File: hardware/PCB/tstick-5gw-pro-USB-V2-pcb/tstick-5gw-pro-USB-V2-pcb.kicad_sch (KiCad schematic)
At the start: 66 parts, among them J1 USB_C_Receptacle_USB2.0, Q1 BSS138, Q2 BSS138, Q3 BSS138, SW1 PTS810 SJM Switch, SW2 PTS810 SJM Switch, U1 USBLC6-2P6, U2 MCP73871, U3 NCP167AMX330TBG, U4 NCP167AMX180TBG

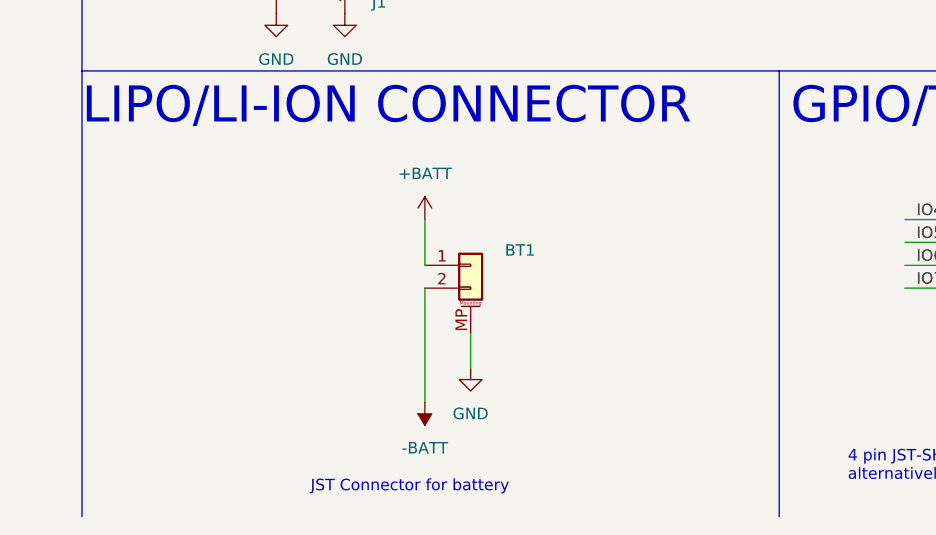
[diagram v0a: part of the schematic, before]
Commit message: updated pcb BOM, switched buttons to smaller 3x2mm buttons
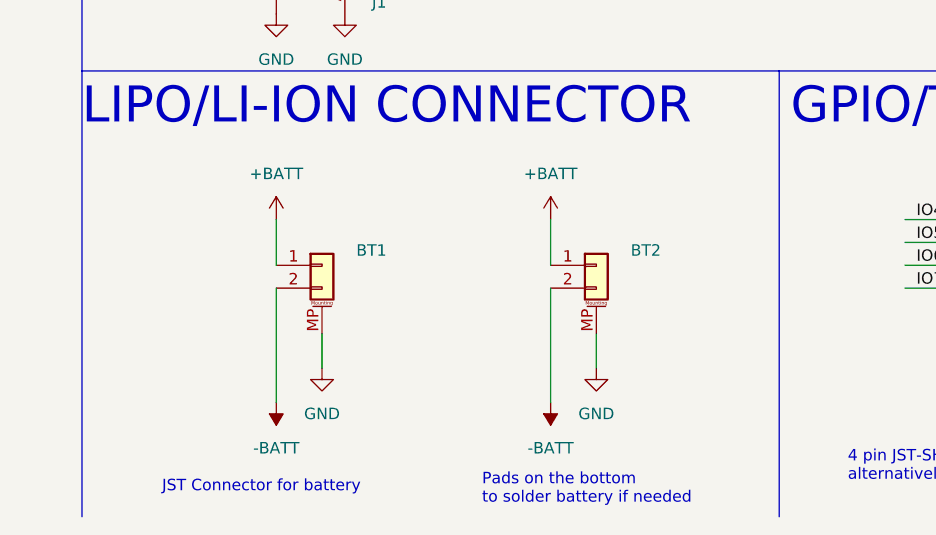
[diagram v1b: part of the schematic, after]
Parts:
- added BT2: JST-PH-1x02-2.000mm, Connector_JST:JST_PH_B2B-PH-SM4-TB_1x02-1MP_P2.00mm_Vertical, symbol Connector_Generic_MountingPin:Conn_01x02_MountingPin
- SW1, SW2: value PTS810 SJM Switch -> B3U-1000P; footprint Button_Switch_SMD:SW_SPST_PTS810 -> Button_Switch_SMD:SW_SPST_B3U-1000P; Manufacturer C&K -> Omron Electronics Inc-EMC Div; Mfg Part # PTS810 SJM 250 SMTR LFS -> B3U-1000P
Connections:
- net +BATT: now also BT2.1 (Pin_1)
- net -BATT: now also BT2.2 (Pin_2)
- net GND: now also BT2.MP (MountPin)
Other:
- note added: "Pads on the bottom to solder battery if needed"
- moved on the sheet: BT1

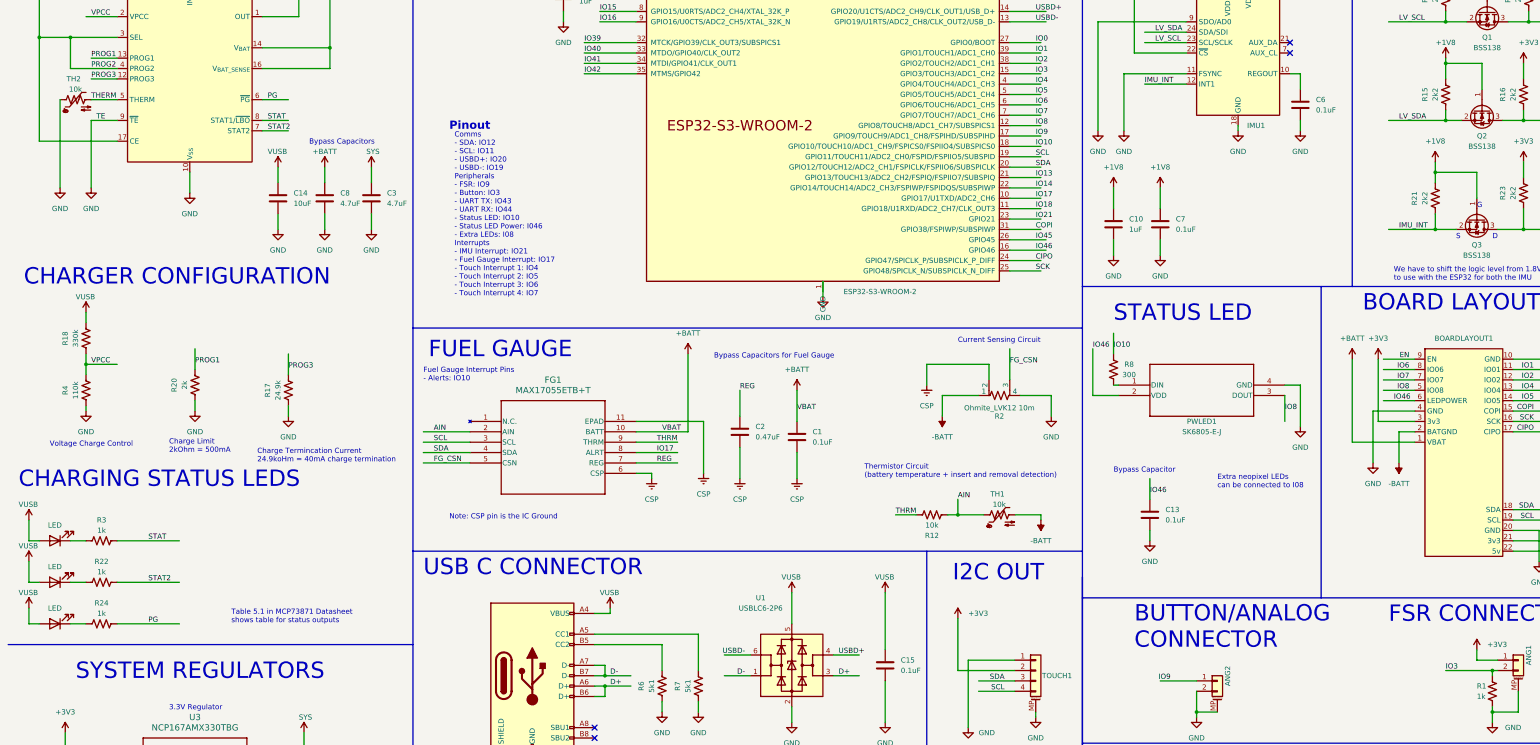
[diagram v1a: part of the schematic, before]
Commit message: updated board flash size, added button interrupt, removed serial print
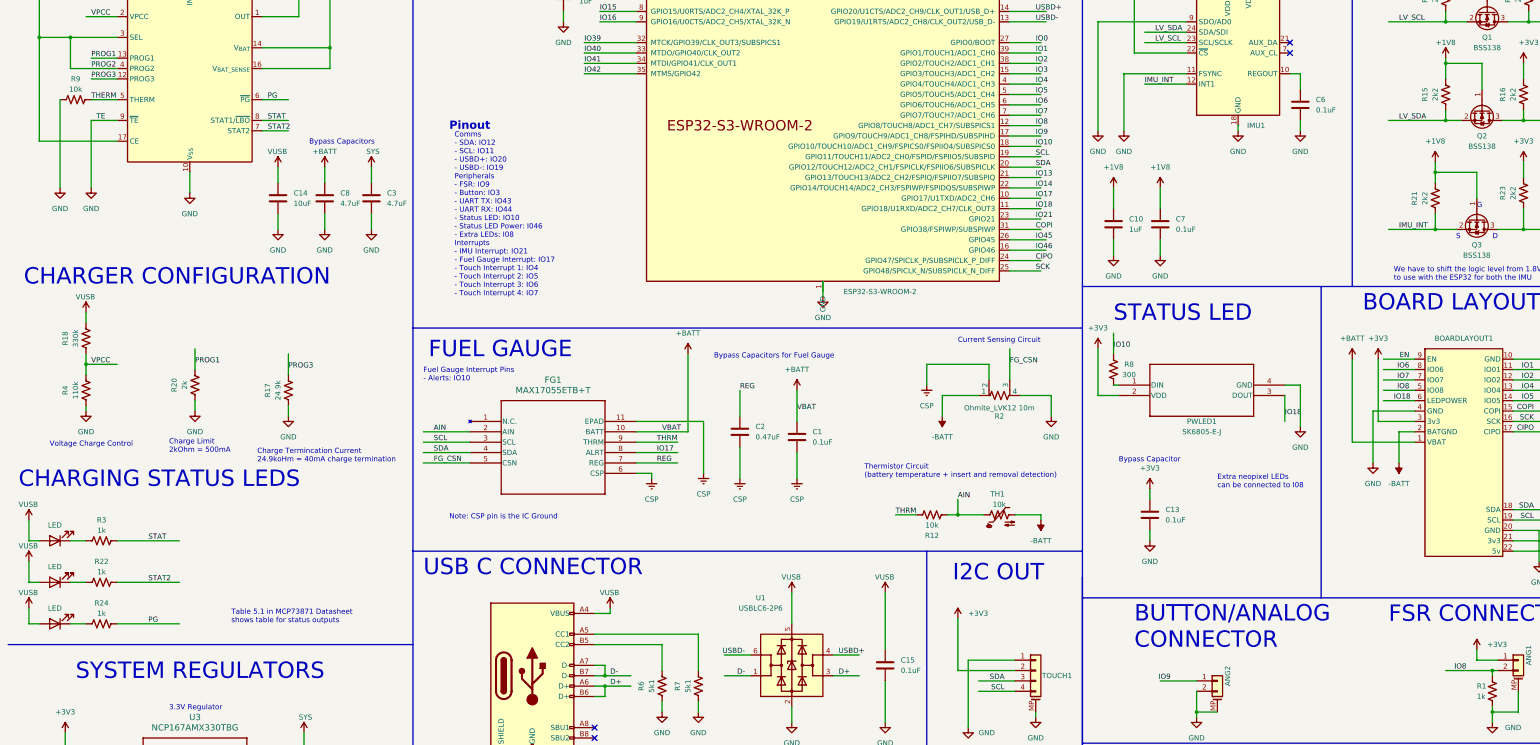
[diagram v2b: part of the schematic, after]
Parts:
- removed TH2: 10k, Resistor_SMD:R_0201_0603Metric, symbol Device:Thermistor_NTC_US
- added R9: 10k, Resistor_SMD:R_0201_0603Metric, symbol Device:R_US
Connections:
- net +3V3: now also C13.1, PWLED1.2 (VDD)
- net GND: now also R9.1
- net IO18: now also BOARDLAYOUT1.6 (LEDPOWER), PWLED1.3 (DOUT)
- net IO3: no longer ANG1.2 (Pin_2), R1.1
- net IO46: no longer BOARDLAYOUT1.6 (LEDPOWER), C13.1, PWLED1.2 (VDD)
- net IO8: now also ANG1.2 (Pin_2), R1.1; no longer PWLED1.3 (DOUT)
- net THERM: now also R9.2
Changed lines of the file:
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@@
     (stroke (width 0) (type default))
   )
-  (wire (pts (xy 276.86 125.73) (xy 276.86 137.16))
+  (wire (pts (xy 278.13 125.73) (xy 278.13 137.16))
     (stroke (width 0) (type default))
   )
@@
     (stroke (width 0) (type default))
   )
-  (wire (pts (xy 290.83 157.48) (xy 290.83 162.56))
+  (wire (pts (xy 290.83 160.02) (xy 290.83 162.56))
     (stroke (width 0) (type default))
   )
@@
     (stroke (width 0) (type default))
   )
-  (wire (pts (xy 276.86 137.16) (xy 283.21 137.16))
+  (wire (pts (xy 278.13 137.16) (xy 283.21 137.16))
     (stroke (width 0) (type default))
   )
@@
     (effects (font (size 1.27 1.27)) (justify left bottom))
   )
-  (text "Bypass Capacitor" (at 281.94 156.21 0)
+  (text "Bypass Capacitor" (at 283.21 153.67 0)
     (effects (font (size 1.27 1.27)) (justify left bottom))
   )
@@
     (effects (font (size 1.27 1.27)) (justify left bottom))
   )
-  (label "IO8" (at 323.85 140.97 0) (fields_autoplaced)
-    (effects (font (size 1.27 1.27)) (justify left bottom))
-  )
   (label "IO3" (at 262.89 58.42 0) (fields_autoplaced)
     (effects (font (size 1.27 1.27)) (justify left bottom))
@@
     (effects (font (size 1.27 1.27)) (justify left bottom))
   )
-  (label "IO46" (at 350.52 138.43 0) (fields_autoplaced)
-    (effects (font (size 1.27 1.27)) (justify left bottom))
-  )
   (label "SCK" (at 262.89 106.68 0) (fields_autoplaced)
     (effects (font (size 1.27 1.27)) (justify left bottom))
@@
     (effects (font (size 1.27 1.27)) (justify left bottom))
   )
-  (label "IO46" (at 290.83 161.29 0) (fields_autoplaced)
-    (effects (font (size 1.27 1.27)) (justify left bottom))
-  )
   (label "SDA" (at 255.27 207.01 180) (fields_autoplaced)
     (effects (font (size 1.27 1.27)) (justify right bottom))
@@
     (effects (font (size 1.27 1.27)) (justify left bottom))
   )
+  (label "IO18" (at 323.85 142.24 0) (fields_autoplaced)
+    (effects (font (size 1.27 1.27)) (justify left bottom))
+  )
   (label "IO7" (at 262.89 68.58 0) (fields_autoplaced)
     (effects (font (size 1.27 1.27)) (justify left bottom))
@@
     (effects (font (size 1.27 1.27)) (justify left bottom))
   )
+  (label "IO18" (at 350.52 138.43 0) (fields_autoplaced)
+    (effects (font (size 1.27 1.27)) (justify left bottom))
+  )
   (label "SCK" (at 384.81 143.51 180) (fields_autoplaced)
     (effects (font (size 1.27 1.27)) (justify right bottom))
@@
     (effects (font (size 1.27 1.27)) (justify right bottom))
   )
-  (label "IO3" (at 363.22 204.47 0) (fields_autoplaced)
-    (effects (font (size 1.27 1.27)) (justify left bottom))
-  )
   (label "VPCC" (at 31.75 129.54 0) (fields_autoplaced)
     (effects (font (size 1.27 1.27)) (justify left bottom))
@@
     (effects (font (size 1.27 1.27)) (justify left bottom))
   )
-  (label "IO46" (at 276.86 125.73 0) (fields_autoplaced)
-    (effects (font (size 1.27 1.27)) (justify left bottom))
-  )
   (label "REG" (at 190.5 135.89 0) (fields_autoplaced)
     (effects (font (size 1.27 1.27)) (justify left bottom))
@@
     (effects (font (size 1.27 1.27)) (justify left bottom))
   )
+  (label "IO8" (at 368.3 204.47 180) (fields_autoplaced)
+    (effects (font (size 1.27 1.27)) (justify right bottom))
+  )
   (label "FG_CSN" (at 256.54 129.54 0) (fields_autoplaced)
     (effects (font (size 1.27 1.27)) (justify left bottom))
@@
     )
   )
-  (symbol (lib_id "Device:Thermistor_NTC_US") (at 27.94 64.77 90) (unit 1)
-    (in_bom yes) (on_board yes) (dnp no)
-    (property "Reference" "TH2" (at 29.21 59.69 90)
-      (effects (font (size 1.27 1.27)) (justify left))
-    )
-    (property "Value" "10k" (at 29.5275 62.23 90)
-      (effects (font (size 1.27 1.27)) (justify left))
-    )
-    (property "Footprint" "Resistor_SMD:R_0201_0603Metric" (at 26.67 64.77 0)
-      (effects (font (size 1.27 1.27)) hide)
-    )
-    (property "Datasheet" "https://industrial.panasonic.com/cdbs/www-data/pdf/AUA0000/AUA0000C8.pdf" (at 26.67 64.77 0)
-      (effects (font (size 1.27 1.27)) hide)
-    )
-    (property "Description Value Pkg" "NTC Thermistor 10k 0201 (0603 Metric)" (at 27.94 64.77 0)
-      (effects (font (size 1.27 1.27)) hide)
-    )
-    (property "Mfg Part #" "ERT-JZEG103FA" (at 27.94 64.77 0)
-      (effects (font (size 1.27 1.27)) hide)
-    )
-    (property "Manufacturer" "Panasonic Electronic Components" (at 27.94 64.77 0)
-      (effects (font (size 1.27 1.27)) hide)
-    )
-    (property "mpn" "ERT-JZEG103FA" (at 27.94 64.77 0)
-      (effects (font (size 1.27 1.27)) hide)
-    )
-    (pin "1")
-    (pin "2")
-    (instances
-      (project "tstick-5gw-pro-USB-V2-pcb"
-        (path "/1e57a4ff-0c95-4e2b-9e56-d9bf8e99c9a1"
-          (reference "TH2") (unit 1)
-        )
-      )
-    )
-  )
   (symbol (lib_id "power:+1V8") (at 363.22 30.48 0) (unit 1)
     (in_bom yes) (on_board yes) (dnp no)
@@
     )
   )
+  (symbol (lib_name "+3V3_2") (lib_id "power:+3V3") (at 290.83 160.02 0) (unit 1)
+    (in_bom yes) (on_board yes) (dnp no) (fields_autoplaced)
+    (property "Reference" "#PWR077" (at 290.83 163.83 0)
+      (effects (font (size 1.27 1.27)) hide)
+    )
+    (property "Value" "+3V3" (at 290.83 154.94 0)
+      (effects (font (size 1.27 1.27)))
+    )
+    (property "Footprint" "" (at 290.83 160.02 0)
+      (effects (font (size 1.27 1.27)) hide)
+    )
+    (property "Datasheet" "" (at 290.83 160.02 0)
+      (effects (font (size 1.27 1.27)) hide)
+    )
+    (property "Description Value Pkg" "" (at 290.83 160.02 0)
+      (effects (font (size 1.27 1.27)) hide)
+    )
+    (property "Mfg Part #" "" (at 290.83 160.02 0)
+      (effects (font (size 1.27 1.27)) hide)
+    )
+    (property "Manufacturer" "" (at 290.83 160.02 0)
+      (effects (font (size 1.27 1.27)) hide)
+    )
+    (pin "1")
+    (instances
+      (project "tstick-5gw-pro-USB-V2-pcb"
+        (path "/1e57a4ff-0c95-4e2b-9e56-d9bf8e99c9a1"
+          (reference "#PWR077") (unit 1)
+        )
+      )
+      (project "tstick_pcb"
+        (path "/ecdbf224-0069-4dc3-a7df-492909ab59c7"
+          (reference "#PWR017") (unit 1)
+        )
+      )
+    )
+  )
   (symbol (lib_name "GND_2") (lib_id "power:GND") (at 327.66 144.78 0) (unit 1)
     (in_bom yes) (on_board yes) (dnp no) (fields_autoplaced)
@@
     )
   )
+  (symbol (lib_id "Device:R_US") (at 27.94 64.77 90) (unit 1)
+    (in_bom yes) (on_board yes) (dnp no)
+    (property "Reference" "R9" (at 27.94 59.69 90)
+      (effects (font (size 1.27 1.27)))
+    )
+    (property "Value" "10k" (at 27.94 62.23 90)
+      (effects (font (size 1.27 1.27)))
+    )
+    (property "Footprint" "Resistor_SMD:R_0201_0603Metric" (at 28.194 63.754 90)
+      (effects (font (size 1.27 1.27)) hide)
+    )
+    (property "Datasheet" "https://industrial.panasonic.com/cdbs/www-data/pdf/RDA0000/AOA0000C304.pdf" (at 27.94 64.77 0)
+      (effects (font (size 1.27 1.27)) hide)
+    )
+    (property "Description Value Pkg" "10 kOhms ±1% 0.05W, 1/20W Chip Resistor 0201 (0603 Metric) Thick Film" (at 27.94 64.77 0)
+      (effects (font (size 1.27 1.27)) hide)
+    )
+    (property "Mfg Part #" "ERJ-1GNF1002C" (at 27.94 64.77 0)
+      (effects (font (size 1.27 1.27)) hide)
+    )
+    (property "Manufacturer" "Panasonic Electronic Components" (at 27.94 64.77 0)
+      (effects (font (size 1.27 1.27)) hide)
+    )
+    (property "mpn" "ERJ-1GNF2492C" (at 27.94 64.77 0)
+      (effects (font (size 1.27 1.27)) hide)
+    )
+    (pin "1")
+    (pin "2")
+    (instances
+      (project "tstick-5gw-pro-USB-V2-pcb"
+        (path "/1e57a4ff-0c95-4e2b-9e56-d9bf8e99c9a1"
+          (reference "R9") (unit 1)
+        )
+      )
+      (project "tstick-4gw-prosumer-pcb"
+        (path "/862dba4e-7e1a-4a09-a4d1-a8449ad175cb"
+          (reference "R6") (unit 1)
+        )
+      )
+      (project "tstick_pcb"
+        (path "/ecdbf224-0069-4dc3-a7df-492909ab59c7"
+          (reference "R10") (unit 1)
+        )
+      )
+    )
+  )
   (symbol (lib_name "GND_1") (lib_id "power:GND") (at 262.89 215.9 0) (unit 1)
     (in_bom yes) (on_board yes) (dnp no) (fields_autoplaced)
@@
         )
       )
+    )
+  )
+  (symbol (lib_name "+3V3_2") (lib_id "power:+3V3") (at 278.13 125.73 0) (unit 1)
+    (in_bom yes) (on_board yes) (dnp no) (fields_autoplaced)
+    (property "Reference" "#PWR076" (at 278.13 129.54 0)
+      (effects (font (size 1.27 1.27)) hide)
+    )
+    (property "Value" "+3V3" (at 278.13 120.65 0)
+      (effects (font (size 1.27 1.27)))
+    )
+    (property "Footprint" "" (at 278.13 125.73 0)
+      (effects (font (size 1.27 1.27)) hide)
+    )
+    (property "Datasheet" "" (at 278.13 125.73 0)
+      (effects (font (size 1.27 1.27)) hide)
+    )
+    (pin "1")
+    (instances
+      (project "tstick-5gw-pro-USB-V2-pcb"
+        (path "/1e57a4ff-0c95-4e2b-9e56-d9bf8e99c9a1"
+          (reference "#PWR076") (unit 1)
+        )
+      )
+      (project "tstick_pcb"
+        (path "/ecdbf224-0069-4dc3-a7df-492909ab59c7"
+          (reference "#PWR017") (unit 1)
+        )
+      )

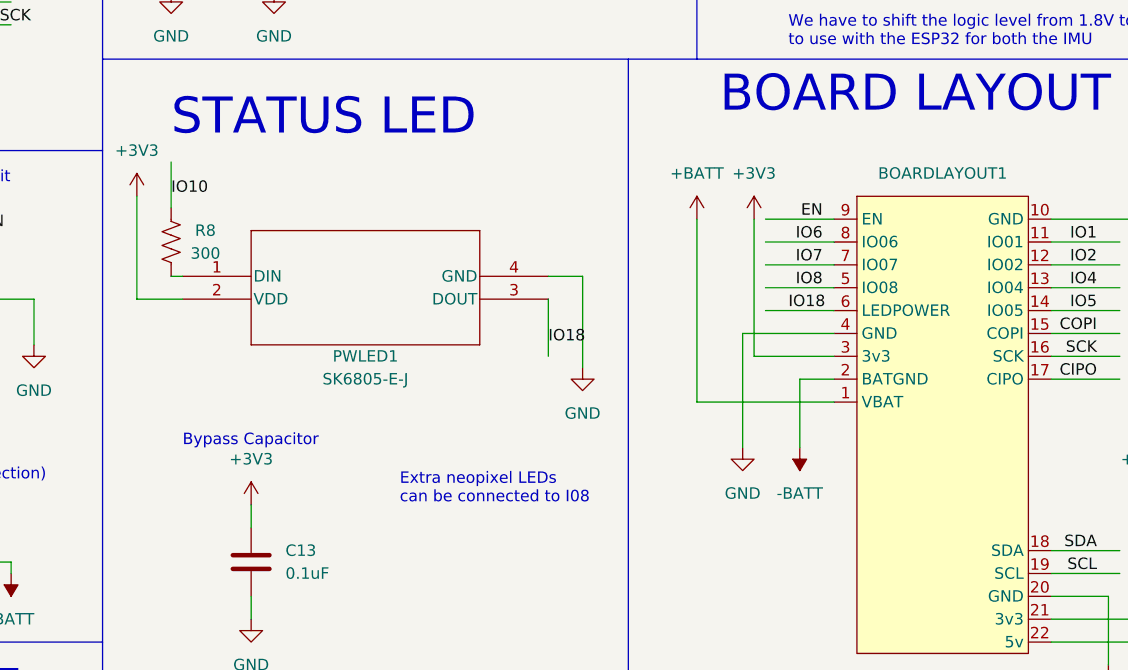
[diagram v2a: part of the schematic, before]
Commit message: removed some LED code, updated schematic, removed choke resistor from both board and BOM
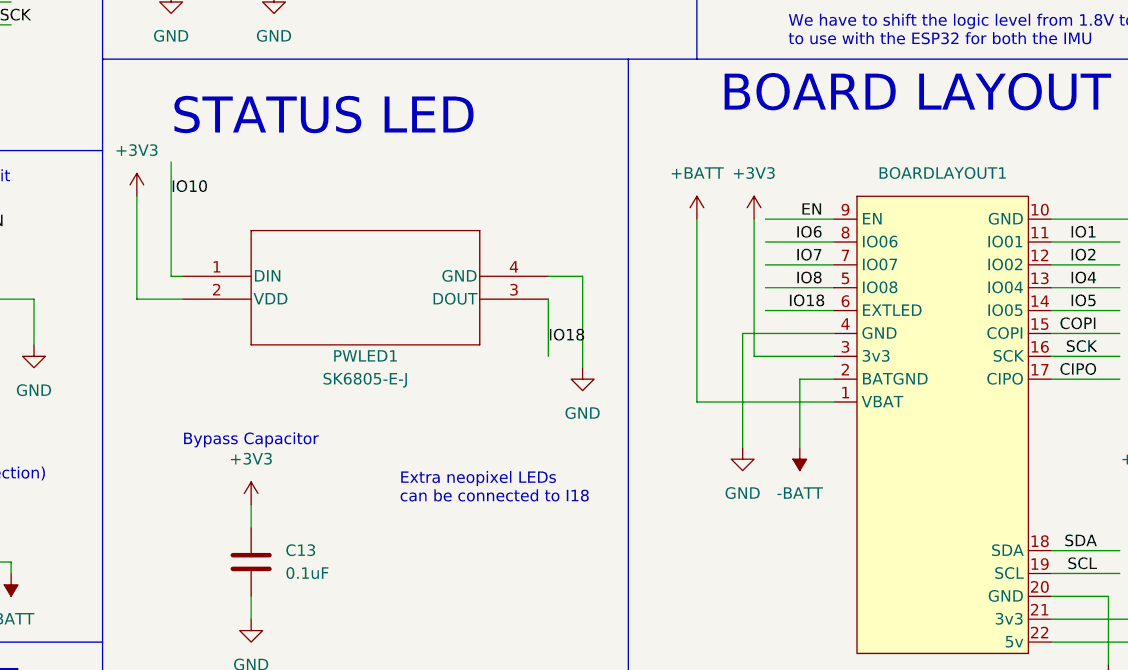
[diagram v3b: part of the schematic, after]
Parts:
- removed R8: 300, Resistor_SMD:R_0201_0603Metric, symbol Device:R_US
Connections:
- net IO10: now also PWLED1.1 (DIN)
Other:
- note added: "Extra neopixel LEDs can be connected to I18"
- note removed: "Extra neopixel LEDs can be connected to I08"
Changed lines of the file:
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@@
     (stroke (width 0) (type default))
   )
-  (wire (pts (xy 281.94 121.92) (xy 281.94 127))
+  (wire (pts (xy 281.94 121.92) (xy 281.94 134.62))
     (stroke (width 0) (type default))
   )
@@
     (effects (font (size 4 4) (color 0 0 0 1)) (justify left bottom))
   )
-  (text "Extra neopixel LEDs \ncan be connected to I08" (at 307.34 160.02 0)
+  (text "Extra neopixel LEDs \ncan be connected to I18" (at 307.34 160.02 0)
     (effects (font (size 1.27 1.27)) (justify left bottom))
   )
@@
         )
       )
-    )
-  )
-  (symbol (lib_id "Device:R_US") (at 281.94 130.81 0) (unit 1)
-    (in_bom yes) (on_board yes) (dnp no)
-    (property "Reference" "R8" (at 285.75 129.54 0)
-      (effects (font (size 1.27 1.27)))
-    )
-    (property "Value" "300" (at 285.75 132.08 0)
-      (effects (font (size 1.27 1.27)))
-    )
-    (property "Footprint" "Resistor_SMD:R_0201_0603Metric" (at 282.956 131.064 90)
-      (effects (font (size 1.27 1.27)) hide)
-    )
-    (property "Datasheet" "https://industrial.panasonic.com/cdbs/www-data/pdf/RDA0000/AOA0000C304.pdf" (at 281.94 130.81 0)
-      (effects (font (size 1.27 1.27)) hide)
-    )
-    (property "Description Value Pkg" "300 Ohms ±1% 0.05W, 1/20W Chip Resistor 0201 (0603 Metric) Thick Film" (at 281.94 130.81 0)
-      (effects (font (size 1.27 1.27)) hide)
-    )
-    (property "Mfg Part #" "ERJ-1GNF3000C" (at 281.94 130.81 0)
-      (effects (font (size 1.27 1.27)) hide)
-    )
-    (property "Manufacturer" "Panasonic Electronic Components" (at 281.94 130.81 0)
-      (effects (font (size 1.27 1.27)) hide)
-    )
-    (property "mpn" "ERJ-1GNF3000C" (at 281.94 130.81 0)
-      (effects (font (size 1.27 1.27)) hide)
-    )
-    (pin "1")
-    (pin "2")
-    (instances
-      (project "tstick-5gw-pro-USB-V2-pcb"
-        (path "/1e57a4ff-0c95-4e2b-9e56-d9bf8e99c9a1"
-          (reference "R8") (unit 1)
-        )
-      )
-      (project "tstick_pcb"
-        (path "/ecdbf224-0069-4dc3-a7df-492909ab59c7"
-          (reference "R10") (unit 1)
-        )
-      )
